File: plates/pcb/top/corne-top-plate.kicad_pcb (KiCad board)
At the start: 2 copper layers, 132.9 x 91.4 mm, 26 parts, among them SW2 KEY_SWITCH

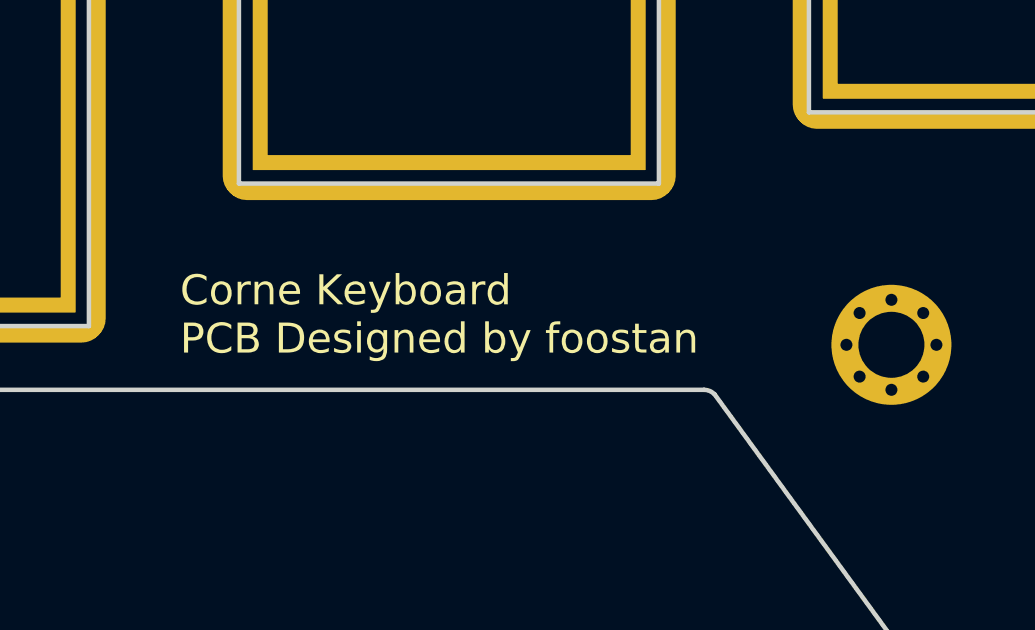
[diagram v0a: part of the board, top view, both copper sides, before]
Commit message: added long design to bottom pbc plate, cleaned up edge cut
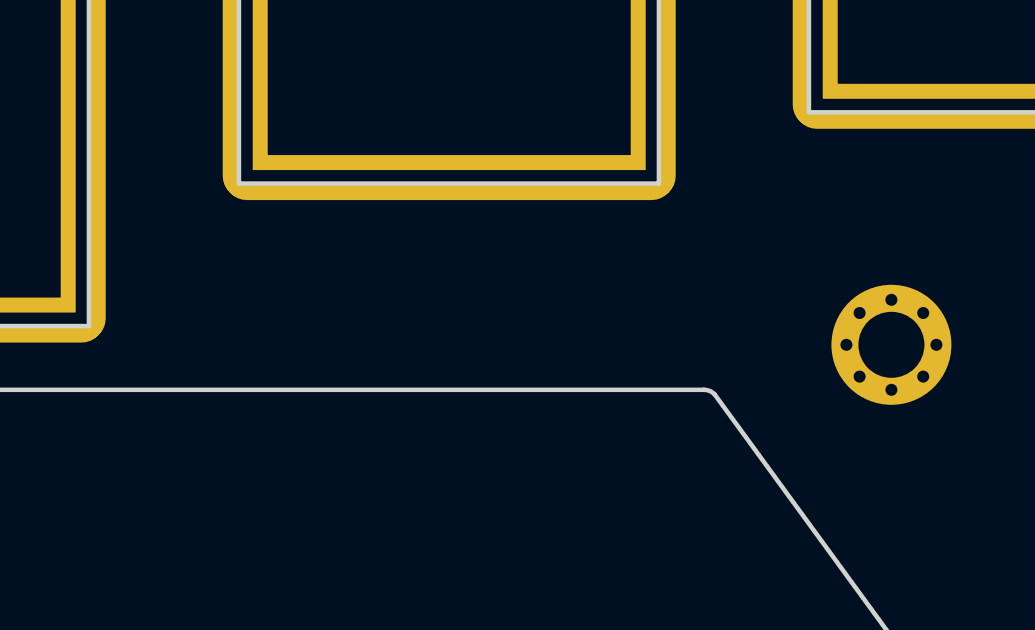
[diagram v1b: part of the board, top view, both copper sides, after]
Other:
- board text removed: "Corne Keyboard PCB Designed by foostan"
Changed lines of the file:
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@@
-(kicad_pcb (version 20171130) (host pcbnew "(5.1.2-1)-1")
+(kicad_pcb (version 20171130) (host pcbnew 5.1.4+dfsg1-1)
   (general
     (thickness 1.6)
-    (drawings 127)
+    (drawings 125)
     (tracks 0)
     (zones 0)
@@
   (gr_line (start 155.51 83) (end 155.5 83) (angle 90) (layer Eco2.User) (width 2.5))
   (gr_line (start 79.5 105.5) (end 79.51 105.5) (angle 90) (layer Eco2.User) (width 2.5))
-  (gr_text "Corne Keyboard\nPCB Designed by foostan" (at 118.406 121.741) (layer B.SilkS)
-    (effects (font (size 1 1) (thickness 0.125)) (justify left mirror))
-  )
-  (gr_text "Corne Keyboard\nPCB Designed by foostan" (at 99.036 121.741) (layer F.SilkS)
-    (effects (font (size 1 1) (thickness 0.125)) (justify left))
-  )
   (gr_line (start 174 66.25) (end 173.997282 116.810192) (angle 90) (layer Edge.Cuts) (width 0.15))
   (gr_arc (start 173.5 66.25) (end 173.5 65.75) (angle 90) (layer Edge.Cuts) (width 0.15))
